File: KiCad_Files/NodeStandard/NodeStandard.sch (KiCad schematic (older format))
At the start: 83 parts, among them J1 EXT1, J10 Force output Relay 2 on, J11 Opto Coupler 3 in, J12 Relay 1 Output, J13 Relay 1 Output, J14 Opto Coupler 1 in, J15 Opto Coupler 2 in, J16 Ext. LED FET 1, J17 Ext. LED FET 2, J18 Schakelaar 1 in, J19 Schakelaar 2 in, J2 EXT2, J20 Schakelaar 3 in, J21 Force output FET 1 on, J22 Force output Relay 1 on, J23 Force output FET 2 on, J24 FET 1 Output, J25 FET 1 Output, J26 230VAC in, J27 5V-in, J28 ExtDC-in, J3 AC Current In, J4 AudioJack3_SwitchTR, J5 AC Current loop, J6 OledDisplay, J7 RFIDReader, J8 Ext. LED Relay 1, J9 Ext. LED Relay 2, K1 SANYOU_SRD_Form_C, K2 SANYOU_SRD_Form_C, Q1 BC547, Q2 BC547, Q3 IRLZ34N, Q4 IRLZ34N, U1 MCP23017_SP

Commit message: V0.3.0.0 Work in progress, layout of components on PCB added
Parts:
- removed J16: Ext. LED FET 1, Connector_Phoenix_MSTB:PhoenixContact_MSTB_2,5_2-GF-5,08_1x02_P5.08mm_Horizontal_ThreadedFlange, symbol Connector:Screw_Terminal_01x02
- removed J17: Ext. LED FET 2, Connector_Phoenix_MSTB:PhoenixContact_MSTB_2,5_2-GF-5,08_1x02_P5.08mm_Horizontal_ThreadedFlange, symbol Connector:Screw_Terminal_01x02
- removed J8: Ext. LED Relay 1, Connector_Phoenix_MSTB:PhoenixContact_MSTB_2,5_2-GF-5,08_1x02_P5.08mm_Horizontal_ThreadedFlange, symbol Connector:Screw_Terminal_01x02
- removed J9: Ext. LED Relay 2, Connector_Phoenix_MSTB:PhoenixContact_MSTB_2,5_2-GF-5,08_1x02_P5.08mm_Horizontal_ThreadedFlange, symbol Connector:Screw_Terminal_01x02
- added C2, C3, C4: 10uF, Capacitor_THT:CP_Radial_D6.3mm_P2.50mm, symbol Device:CP
- added C8: 100uF, Capacitor_THT:CP_Radial_D6.3mm_P2.50mm, symbol Device:CP
- added C9: 2n2, Capacitor_THT:C_Disc_D5.1mm_W3.2mm_P5.00mm, symbol Device:C
- added D1, D10, D11, D12, D2, D7, D8, D9: 1N4148, Diode_THT:D_DO-35_SOD27_P7.62mm_Horizontal, symbol Diode:1N4148
- added D17: LED, LED_THT:LED_D3.0mm, symbol Device:LED
- added D18: 1N4004, Diode_THT:D_DO-41_SOD81_P10.16mm_Horizontal, symbol Diode:1N4004
- added J22: Force output Relay 3 on, Connector_PinHeader_2.54mm:PinHeader_1x02_P2.54mm_Vertical, symbol Connector_Generic:Conn_01x02
- added J23: Relay 3 Output 1, Connector_Phoenix_MSTB:PhoenixContact_MSTB_2,5_3-GF-5,08_1x03_P5.08mm_Horizontal_ThreadedFlange, symbol Connector:Screw_Terminal_01x03
- added J24: Relay 3 Output 2, Connector_Phoenix_MSTB:PhoenixContact_MSTB_2,5_3-GF-5,08_1x03_P5.08mm_Horizontal_ThreadedFlange, symbol Connector:Screw_Terminal_01x03
- added JP8: 230VAC-L, Jumper:SolderJumper-2_P1.3mm_Open_RoundedPad1.0x1.5mm, symbol Jumper:SolderJumper_2_Open
- added K3: RT42xAxx, Relay_THT:Relay_DPDT_Schrack-RT2-FormC_RM5mm, symbol Relay:RT42xAxx
- added Q5: BC547, Package_TO_SOT_THT:TO-92_Inline, symbol Transistor_BJT:BC547
- added R28: 1k, Resistor_THT:R_Axial_DIN0207_L6.3mm_D2.5mm_P7.62mm_Horizontal, symbol Device:R
- added R29, R3: 2k2, Resistor_THT:R_Axial_DIN0207_L6.3mm_D2.5mm_P7.62mm_Horizontal, symbol Device:R
- added R7, R8: 10k, Resistor_THT:R_Axial_DIN0207_L6.3mm_D2.5mm_P7.62mm_Horizontal, symbol Device:R
- C1: renamed from C2; footprint (none) -> Capacitor_THT:CP_Radial_D6.3mm_P2.50mm
- J14: renamed from J13; value Relay 1 Output -> Relay 2 Output
- J2: renamed from J4; footprint (none) -> Jack_3.5mm_CUI_FEMPM_Horizontal
- J20: renamed from J24; footprint TerminalBlock_RND:TerminalBlock_RND_205-00288_1x03_P5.08mm_Horizontal -> Connector_Phoenix_MSTB:PhoenixContact_MSTB_2,5_4-GF-5,08_1x04_P5.08mm_Horizontal_ThreadedFlange
- JP1, JP2, JP3, JP4, JP5, JP6, JP7: footprint (none) -> Jumper:SolderJumper-2_P1.3mm_Open_RoundedPad1.0x1.5mm
- L1: footprint (none) -> Footprints:TA12-100
- OK1, OK2, OK3: footprint PC814:DIL04 -> Footprints:DIL04
- R13: renamed from R7; footprint Resistor_THT:R_Axial_DIN0207_L6.3mm_D2.5mm_P7.62mm_Horizontal -> Resistor_THT:R_Axial_DIN0516_L15.5mm_D5.0mm_P20.32mm_Horizontal
- R14: renamed from R6; footprint Resistor_THT:R_Axial_DIN0207_L6.3mm_D2.5mm_P7.62mm_Horizontal -> Resistor_THT:R_Axial_DIN0516_L15.5mm_D5.0mm_P20.32mm_Horizontal
- R15: renamed from R9; footprint Resistor_THT:R_Axial_DIN0207_L6.3mm_D2.5mm_P7.62mm_Horizontal -> Resistor_THT:R_Axial_DIN0516_L15.5mm_D5.0mm_P20.32mm_Horizontal
- R16: renamed from R8; footprint Resistor_THT:R_Axial_DIN0207_L6.3mm_D2.5mm_P7.62mm_Horizontal -> Resistor_THT:R_Axial_DIN0516_L15.5mm_D5.0mm_P20.32mm_Horizontal
- R17: renamed from R15; footprint Resistor_THT:R_Axial_DIN0207_L6.3mm_D2.5mm_P7.62mm_Horizontal -> Resistor_THT:R_Axial_DIN0516_L15.5mm_D5.0mm_P20.32mm_Horizontal
- R18: renamed from R16; footprint Resistor_THT:R_Axial_DIN0207_L6.3mm_D2.5mm_P7.62mm_Horizontal -> Resistor_THT:R_Axial_DIN0516_L15.5mm_D5.0mm_P20.32mm_Horizontal
- renumbered C4 to C5, C3 to C6, C1 to C7, D5 to D13, D6 to D14, D7 to D15, D8 to D16, D2 to D4, D1 to D5, D4 to D6, J3 to J1, J14 to J10, J15 to J11, J11 to J12, J12 to J13, J20 to J15, J19 to J16, J18 to J17, J21 to J18, J23 to J19, J25 to J21, J26 to J25, J27 to J26, J28 to J27, J5 to J3, J1 to J4, J6 to J5, J7 to J6, J2 to J7, J22 to J8, J10 to J9, Q2 to Q1, Q1 to Q2, R13 to R10, R10 to R11, R14 to R12, R20 to R19, R19 to R20, R3 to R21, R17 to R22, R18 to R23, R21 to R24, R22 to R25, R23 to R26, R24 to R27, R12 to R6, R11 to R9
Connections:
- net +3V3: now also D1.1 (K), D11.1 (K), D7.1 (K), D9.1 (K), R7.1, R8.1
- net +5V: now also J26.1 (Pin_1), C8.1, C9.1, D18.1 (K), K3.A1, R29.1; no longer J26.2 (Pin_2)
- net 230VAC-L: now also J25.1 (Pin_1), JP8.2 (B); no longer J25.2 (Pin_2)
- net 230VAC-N: now also J25.2 (Pin_2); no longer J25.1 (Pin_1)
- net ExternalDCPower: now also J27.1 (Pin_1); no longer J27.2 (Pin_2)
- net FET1: now also U1.4 (GPB3); no longer U1.3 (GPB2)
- net FET2: now also U1.5 (GPB4); no longer U1.4 (GPB3)
- net GND: now also J26.2 (Pin_2), J27.2 (Pin_2), C2.2, C3.2, C4.2, C8.2, C9.2, D10.2 (A), D12.2 (A), D2.2 (A), D8.2 (A), J22.2 (Pin_2), Q5.3 (E); no longer J26.1 (Pin_1), J27.1 (Pin_1)
- net GPI35: now also D1.2 (A), D2.1 (K), R3.1; no longer J2.S, L1.2, R1.1
- net GPI36_U1RXD: now also C4.1
- net GPIO32: now also C2.1, R7.2
- net GPIO33: now also C3.1, R8.2
- net Switch1: now also D7.2 (A), D8.1 (K)
- net Switch2: now also D10.1 (K), D9.2 (A)
- net Switch3: now also D11.2 (A), D12.1 (K)
- net at J13.1 (Pin_1): now also K1.3; no longer K1.4
- net at J13.3 (Pin_3): now also K1.4; no longer K1.3
- net at OK1.2 (AC2), R14.2: no longer JP1.1 (A)
- net at J10.1 (Pin_1): now also R13.1; no longer R14.1
- net at J10.2 (Pin_2): now also JP1.1 (A), R14.1; no longer R13.1
- net at OK2.2 (AC2), R16.2: no longer JP2.1 (A)
- net at J11.1 (Pin_1): now also R15.1; no longer R16.1
- net at J11.2 (Pin_2): now also JP2.1 (A), R16.1; no longer R15.1
- net at OK3.2 (AC2), R18.2: no longer JP3.1 (A)
- net at J12.1 (Pin_1): now also R17.1; no longer R18.1
- net at J12.2 (Pin_2): now also JP3.1 (A), R18.1; no longer R17.1
- net at J1.1 (Pin_1): now also J3.2 (Pin_2); no longer J3.1 (Pin_1)
- net at J1.2 (Pin_2): now also J3.1 (Pin_1); no longer J3.2 (Pin_2)
- net at J14.1 (Pin_1): now also K2.3; no longer K2.4
- net at J14.3 (Pin_3): now also K2.4; no longer K2.3
- new net: J2.S, L1.2, R1.1, R3.2
- new net: J23.2 (Pin_2), K3.11
- new net: J23.1 (Pin_1), K3.12
- new net: J23.3 (Pin_3), K3.14
- new net: J24.2 (Pin_2), JP8.1 (A), K3.21
- new net: J24.3 (Pin_3), K3.22
- new net: J24.1 (Pin_1), K3.24
- new net: D17.1 (K), D18.2 (A), J22.1 (Pin_1), K3.A2, Q5.1 (C)
- new net: D17.2 (A), R29.2
- new net: Q5.2 (B), R28.1
- new net Relay3: R28.2, U1.3 (GPB2)
- no-connect marks 24 -> 23
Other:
- note added: "Relay 3 output"
- note removed: "LED-A"
- note removed: "LED-K"
- moved on the sheet: C5, C6, C7, D14, D16, J10, J12, J15, J16, J17, J19, J21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

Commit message: V0.4 Work in progress, added some footprints with 3D models
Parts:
- J3: footprint TerminalBlock_RND:TerminalBlock_RND_205-00287_1x02_P5.08mm_Horizontal -> TerminalBlock_Phoenix:TerminalBlock_Phoenix_MKDS-1,5-2-5.08_1x02_P5.08mm_Horizontal
- OK1, OK2, OK3: footprint Footprints:DIL04 -> Package_DIP:DIP-4_W7.62mm
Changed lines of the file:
@@
 Title "Node Standard"
 Date "2020-11-23"
-Rev "V0.3"
+Rev "V0.4"
 Comp "MakerSpace Leiden"
 Comment1 "Getekend door: Hans Beerman"
@@
 F 0 "OK1" H 6450 7170 50  0000 C CNN
 F 1 "PC814" H 6450 7079 50  0000 C CNN
-F 2 "Footprints:DIL04" H 6400 6800 50  0000 L BNN
+F 2 "Package_DIP:DIP-4_W7.62mm" H 6400 6800 50  0000 L BNN
 F 3 "" H 6400 6800 50  0001 L BNN
 F 4 "unknown" H 6400 6800 50  0001 L BNN "Field4"
@@
 F 0 "OK2" H 6450 8670 50  0000 C CNN
 F 1 "PC814" H 6450 8579 50  0000 C CNN
-F 2 "Footprints:DIL04" H 6400 8300 50  0001 L BNN
+F 2 "Package_DIP:DIP-4_W7.62mm" H 6400 8300 50  0001 L BNN
 F 3 "" H 6400 8300 50  0001 L BNN
 F 4 "unknown" H 6400 8300 50  0001 L BNN "Field4"
@@
 F 0 "OK3" H 6450 10070 50  0000 C CNN
 F 1 "PC814" H 6450 9979 50  0000 C CNN
-F 2 "Footprints:DIL04" H 6400 9700 50  0001 L BNN
+F 2 "Package_DIP:DIP-4_W7.62mm" H 6400 9700 50  0001 L BNN
 F 3 "" H 6400 9700 50  0001 L BNN
 F 4 "unknown" H 6400 9700 50  0001 L BNN "Field4"
@@
 F 0 "J3" H 2430 6380 50  0000 L CNN
 F 1 "AC Current loop" H 2170 6780 50  0000 L CNN
-F 2 "TerminalBlock_RND:TerminalBlock_RND_205-00287_1x02_P5.08mm_Horizontal" H 2475 6625 50  0001 C CNN
+F 2 "TerminalBlock_Phoenix:TerminalBlock_Phoenix_MKDS-1,5-2-5.08_1x02_P5.08mm_Horizontal" H 2475 6625 50  0001 C CNN
 F 3 "~" H 2475 6625 50  0001 C CNN
 	1    2475 6625

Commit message: V0.5 Work in progress, first version  PCB design, no silk screen yet
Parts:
- added J28: Hal current sensor, TerminalBlock_Phoenix:TerminalBlock_Phoenix_MPT-0,5-3-2.54_1x03_P2.54mm_Horizontal, symbol Connector:Screw_Terminal_01x03
- added J29: Current sensor select, Connector_PinHeader_2.54mm:PinHeader_1x03_P2.54mm_Vertical, symbol Connector_Generic:Conn_01x03
- J15, J16, J17: footprint Connector_Phoenix_MSTB:PhoenixContact_MSTB_2,5_2-GF-5,08_1x02_P5.08mm_Horizontal_ThreadedFlange -> TerminalBlock_Phoenix:TerminalBlock_Phoenix_MPT-0,5-2-2.54_1x02_P2.54mm_Horizontal
- J5, J6: footprint Connector_Phoenix_MSTB:PhoenixContact_MSTB_2,5_4-GF-5,08_1x04_P5.08mm_Horizontal_ThreadedFlange -> TerminalBlock_Phoenix:TerminalBlock_Phoenix_MPT-0,5-4-2.54_1x04_P2.54mm_Horizontal
- JP1, JP2, JP3, JP4, JP5, JP8: footprint Jumper:SolderJumper-2_P1.3mm_Open_RoundedPad1.0x1.5mm -> Footprints:SolderJumper-2_P3mm_Open_RoundedPad
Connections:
- net +3V3: now also J28.1 (Pin_1)
- net 230VAC-L: now also J25.2 (Pin_2); no longer J25.1 (Pin_1)
- net 230VAC-N: now also J25.1 (Pin_1); no longer J25.2 (Pin_2)
- net GND: now also J28.2 (Pin_2)
- net GPI35: now also J29.2 (Pin_2); no longer D1.2 (A), D2.1 (K), R3.1
- new net: D1.2 (A), D2.1 (K), J29.3 (Pin_3), R3.1
- new net: J28.3 (Pin_3), J29.1 (Pin_1)
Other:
- moved on the sheet: C1, D1, D2, J1, J2, J3, J4, J5, J6, J7, L1, R1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

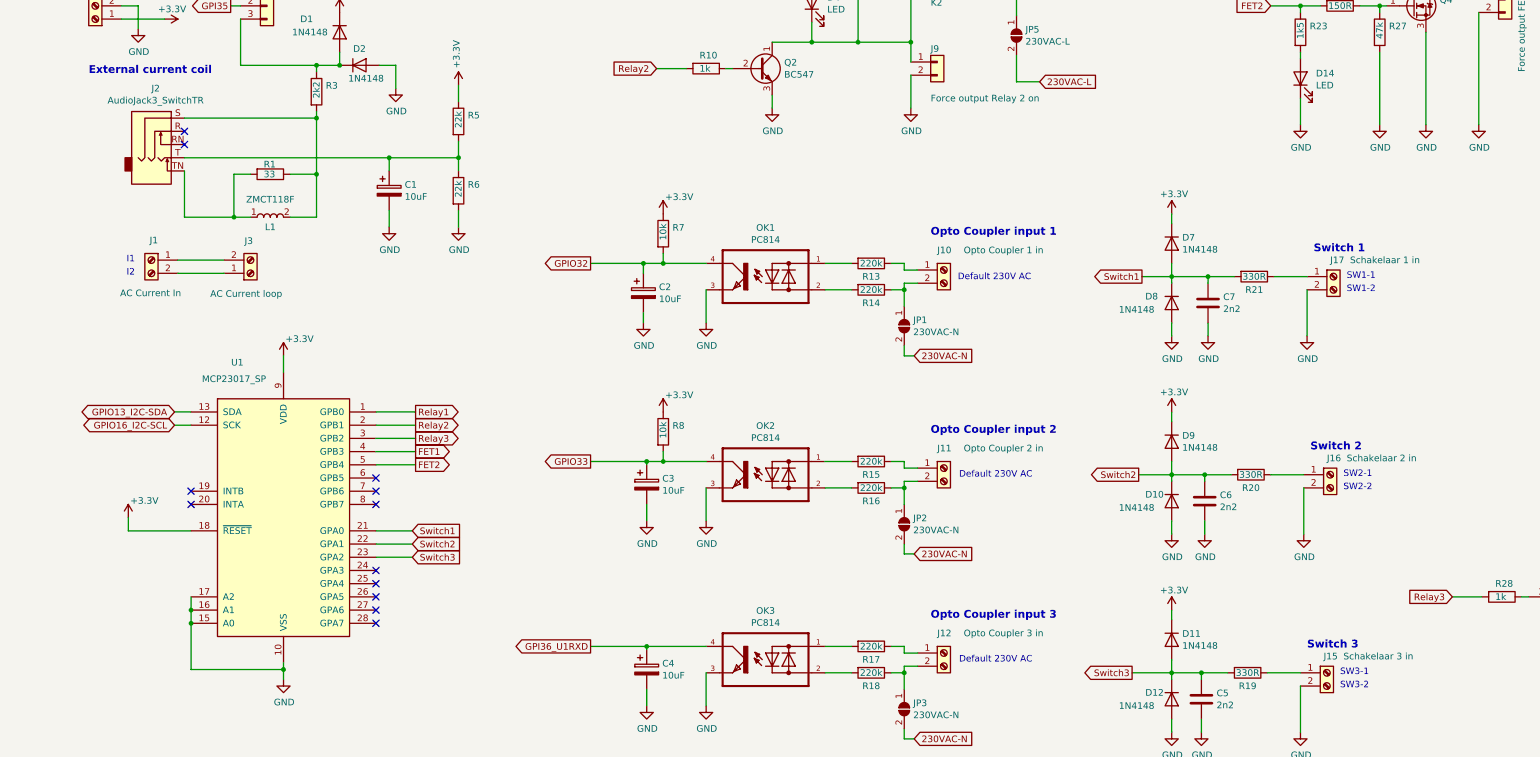
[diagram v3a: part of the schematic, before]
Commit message: V0.6 Silk screen added, ready for first trial with real print
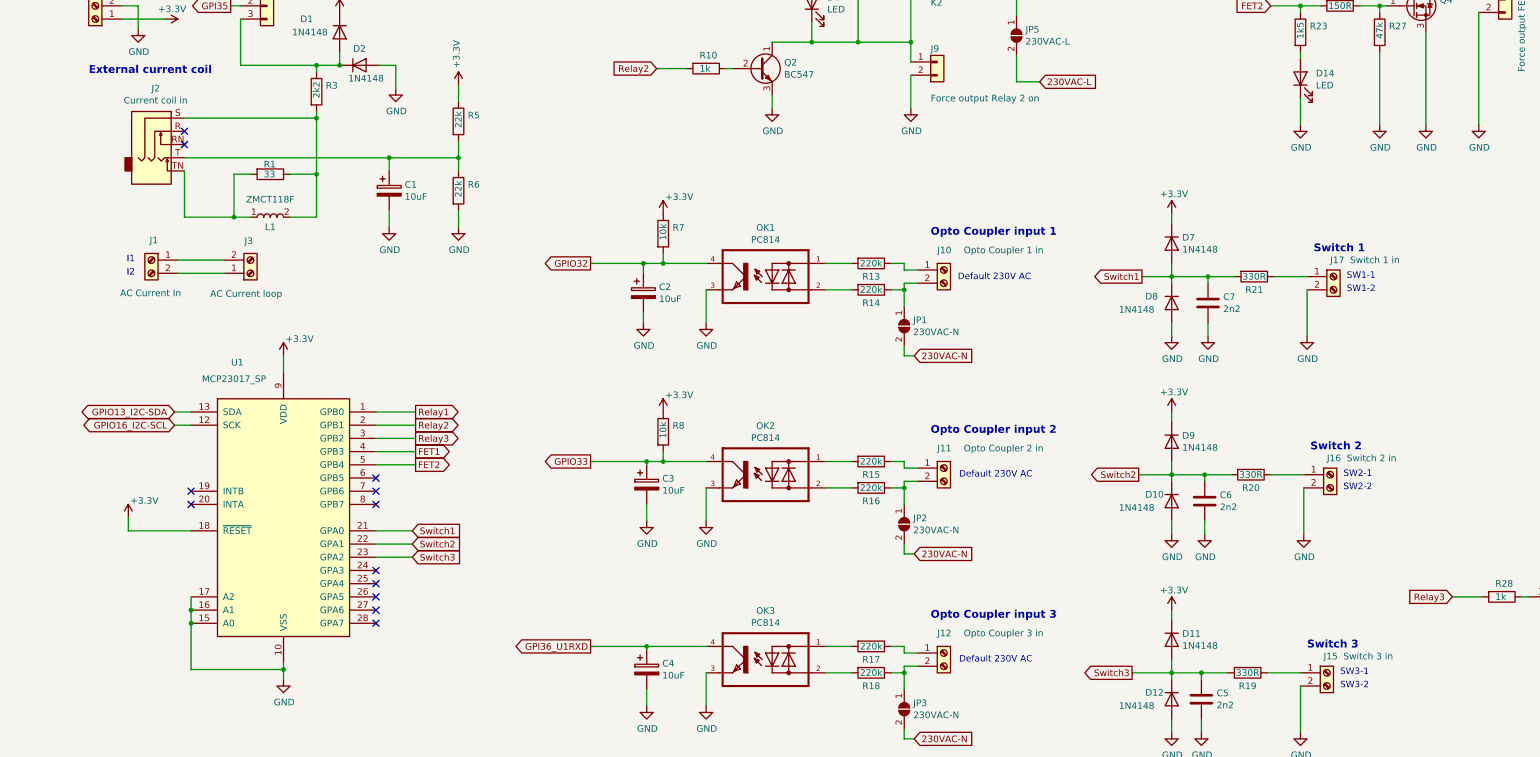
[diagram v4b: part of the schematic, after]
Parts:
- J15: value Schakelaar 3 in -> Switch 3 in
- J16: value Schakelaar 2 in -> Switch 2 in
- J17: value Schakelaar 1 in -> Switch 1 in
- J2: value AudioJack3_SwitchTR -> Current coil in
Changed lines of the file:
@@
 Sheet 1 1
 Title "Node Standard"
-Date "2020-12-04"
-Rev "V0.5"
+Date "2020-12-10"
+Rev "V0.6"
 Comp "MakerSpace Leiden"
 Comment1 "Getekend door: Hans Beerman"
@@
 P 1750 5700
 F 0 "J2" H 1732 6025 50  0000 C CNN
-F 1 "AudioJack3_SwitchTR" H 1732 5934 50  0000 C CNN
+F 1 "Current coil in" H 1732 5934 50  0000 C CNN
 F 2 "Jack_3.5mm_CUI_FEMPM_Horizontal" H 1750 5700 50  0001 C CNN
 F 3 "~" H 1750 5700 50  0001 C CNN
@@
 P 10650 6800
 F 0 "J17" H 10625 6925 50  0000 L CNN
-F 1 "Schakelaar 1 in" H 10775 6925 50  0000 L CNN
+F 1 "Switch 1 in" H 10775 6925 50  0000 L CNN
 F 2 "TerminalBlock_Phoenix:TerminalBlock_Phoenix_MPT-0,5-2-2.54_1x02_P2.54mm_Horizontal" H 10650 6800 50  0001 C CNN
 F 3 "~" H 10650 6800 50  0001 C CNN
@@
 P 10625 8300
 F 0 "J16" H 10600 8425 50  0000 L CNN
-F 1 "Schakelaar 2 in" H 10750 8425 50  0000 L CNN
+F 1 "Switch 2 in" H 10750 8425 50  0000 L CNN
 F 2 "TerminalBlock_Phoenix:TerminalBlock_Phoenix_MPT-0,5-2-2.54_1x02_P2.54mm_Horizontal" H 10625 8300 50  0001 C CNN
 F 3 "~" H 10625 8300 50  0001 C CNN
@@
 P 10600 9800
 F 0 "J15" H 10575 9925 50  0000 L CNN
-F 1 "Schakelaar 3 in" H 10725 9925 50  0000 L CNN
+F 1 "Switch 3 in" H 10725 9925 50  0000 L CNN
 F 2 "TerminalBlock_Phoenix:TerminalBlock_Phoenix_MPT-0,5-2-2.54_1x02_P2.54mm_Horizontal" H 10600 9800 50  0001 C CNN
 F 3 "~" H 10600 9800 50  0001 C CNN

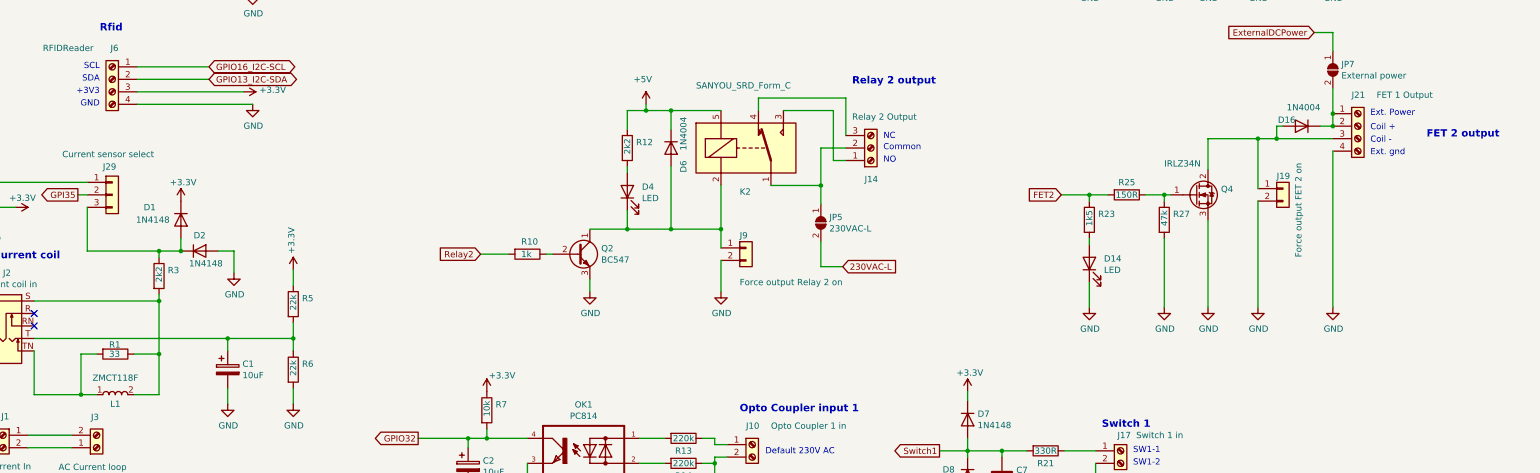
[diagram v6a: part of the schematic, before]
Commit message: Version 0.9: 2 typo's in silkscreen labels corrected
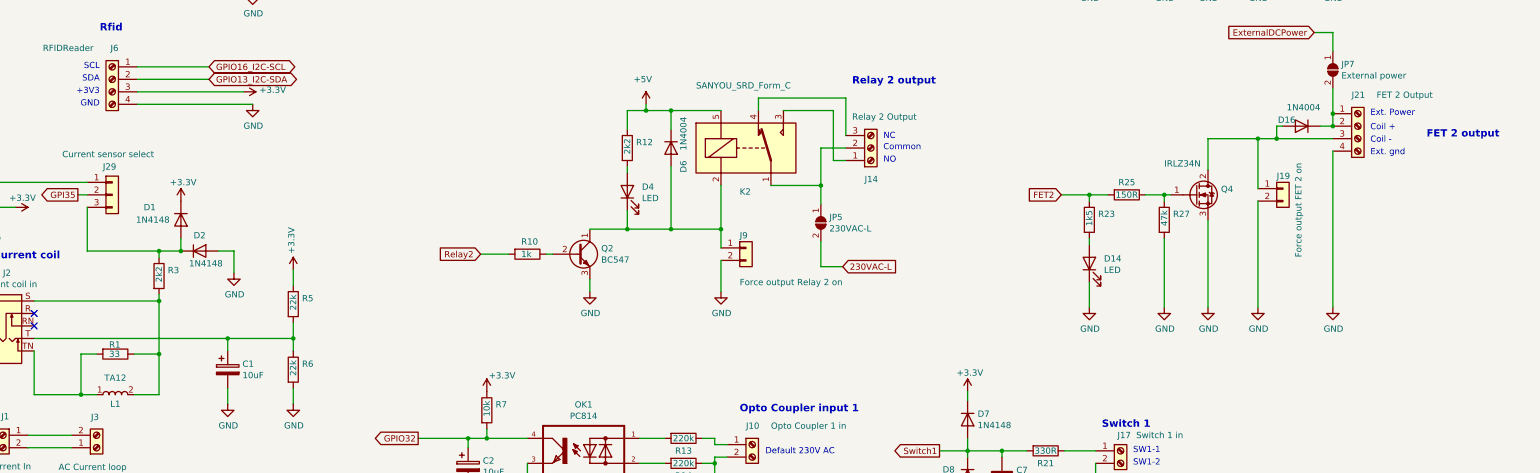
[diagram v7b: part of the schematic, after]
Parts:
- J21: value FET 1 Output -> FET 2 Output
- L1: value ZMCT118F -> TA12
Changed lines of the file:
@@
 Sheet 1 1
 Title "Node Standard"
-Date "2021-01-06"
-Rev "V0.8"
+Date "2021-02-18"
+Rev "V0.9"
 Comp "MakerSpace Leiden"
 Comment1 "Getekend door: Hans Beerman"
@@
 P 12550 4200
 F 0 "J21" H 12500 4450 50  0000 L CNN
-F 1 "FET 1 Output" H 12700 4450 50  0000 L CNN
+F 1 "FET 2 Output" H 12700 4450 50  0000 L CNN
 F 2 "Connector_Phoenix_MSTB:PhoenixContact_MSTB_2,5_4-GF-5,08_1x04_P5.08mm_Horizontal_ThreadedFlange" H 12550 4200 50  0001 C CNN
 F 3 "~" H 12550 4200 50  0001 C CNN
@@
 P 2600 6350
 F 0 "L1" V 2525 6350 50  0000 C CNN
-F 1 "ZMCT118F" V 2734 6350 50  0000 C CNN
+F 1 "TA12" V 2734 6350 50  0000 C CNN
 F 2 "Footprints:TA12-100" H 2600 6350 50  0001 C CNN
 F 3 "~" H 2600 6350 50  0001 C CNN
